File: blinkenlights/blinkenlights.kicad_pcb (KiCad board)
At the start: 4 copper layers, 160 x 100 mm, 158 parts, among them J201 Conn_03x32_Row_Letter_First, J301 Conn_01x01_Female, J302 Conn_01x01_Female, J303 Conn_01x01_Female, J304 Conn_01x01_Female, J501 Conn_ARM_SWD, J502 Conn_02x03_Odd_Even, SW101 Black, SW102 Orang, U104 74AUC2G07, U106 74HC2G14, U301 BD9C301FJ, U303 AMS1117-3.3, U401 74HC244, U402 74AUC2G34, U501 ATSAM4S8CB-AN, U502 PCA9306DP, U601 SN74LVCH16T245, U602 SN74LXC8T245, U603 SN74LVC2T45, U604 SN74LVC2T45, U605 SN74LVC2T45, U606 SN74LVCH16T245, U607 SN74LXC8T245, U608 74LVC2G06, U609 74LVC2G06, U610 74LVC2G06, U611 74LVC2G06

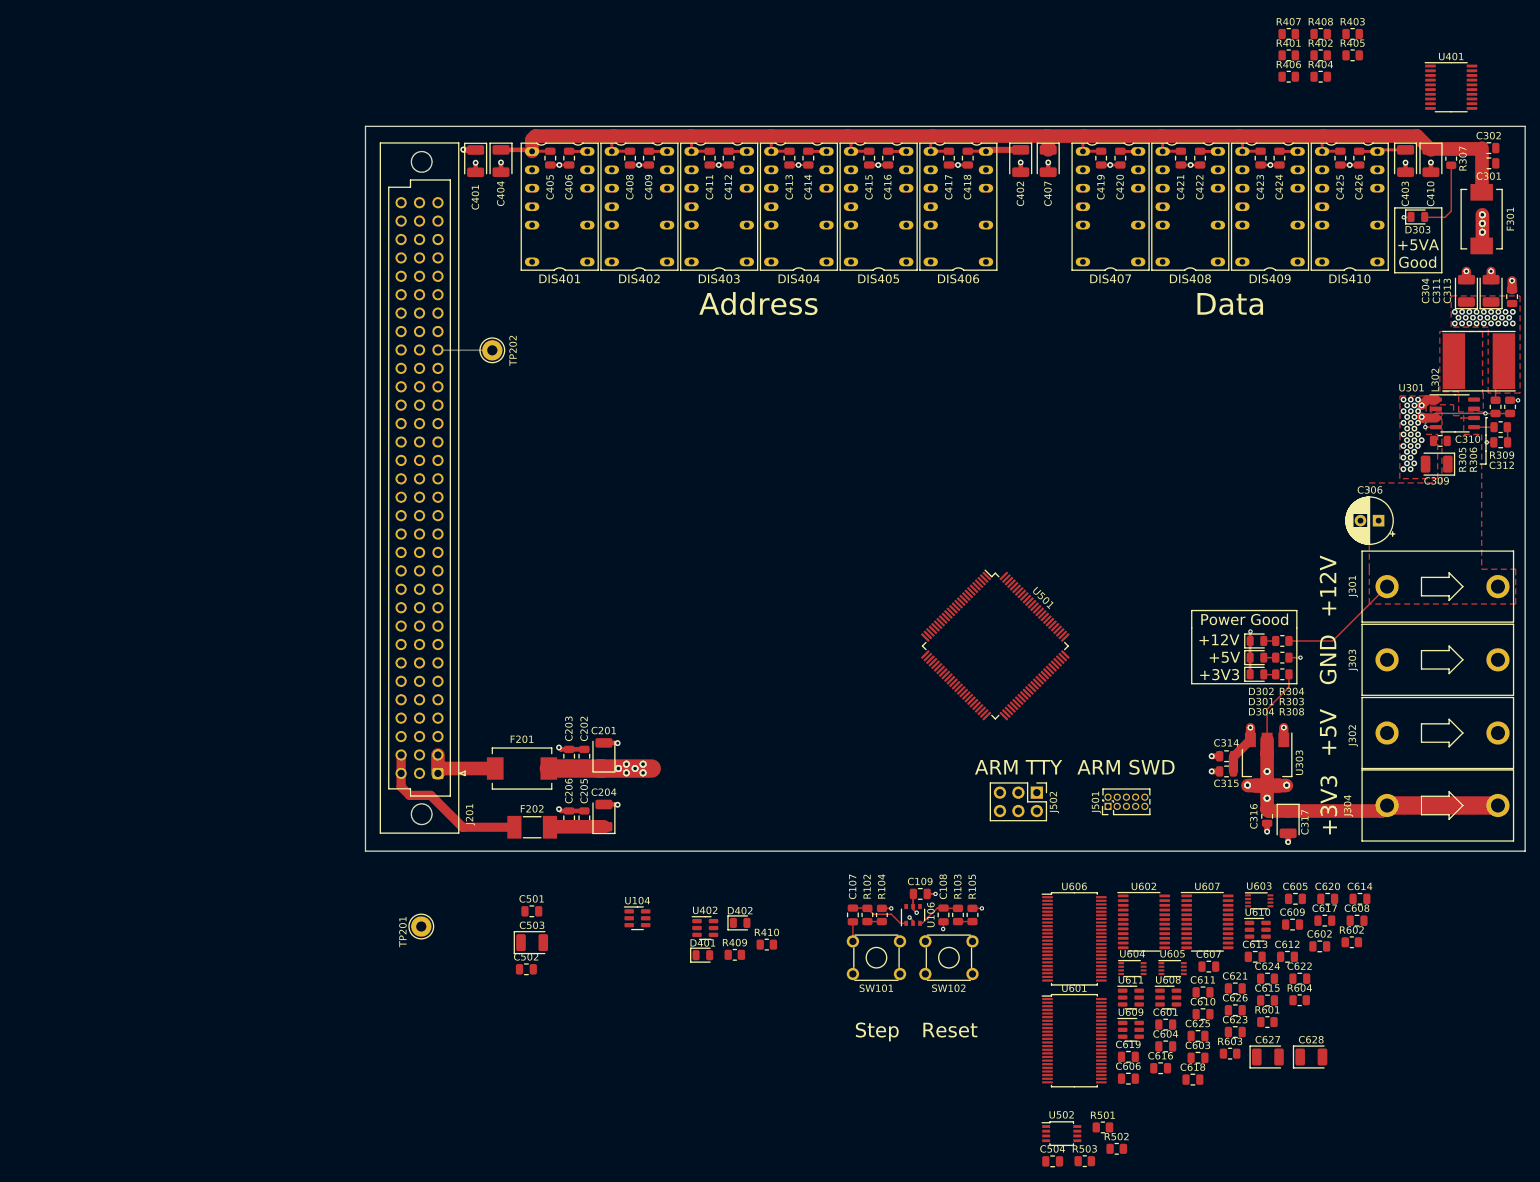
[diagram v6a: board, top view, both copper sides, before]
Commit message: Routed address/data bus on blinkenlights
- It goes to the funky hex display bois now and is routed so that it
  should be pretty ez to yeet on down into level shifters for the big
  ARM chip that runs the show
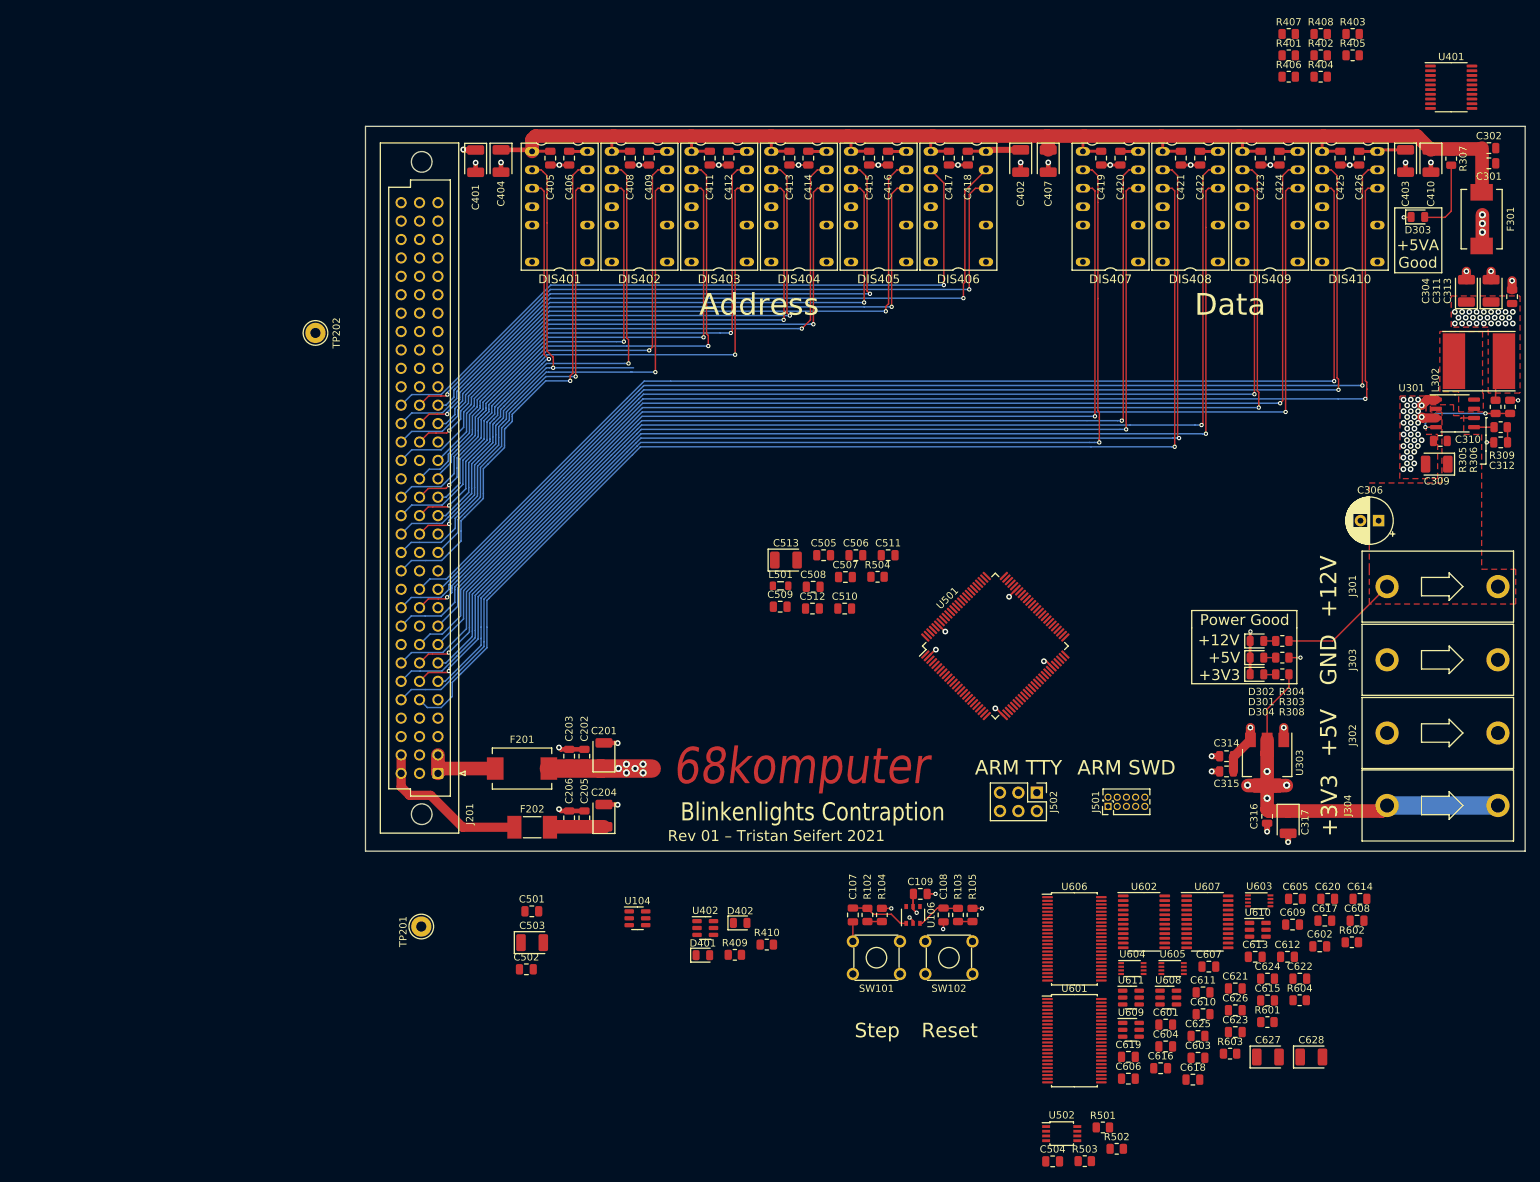
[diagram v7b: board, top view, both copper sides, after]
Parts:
- added C505: 100nF, Capacitor_SMD:C_0805_2012Metric, F.Cu at (83.2, 79.2)
- added C506: 100nF, Capacitor_SMD:C_0805_2012Metric, F.Cu at (87.7, 79.2)
- added C507: 100nF, Capacitor_SMD:C_0805_2012Metric, F.Cu at (86.2, 82.2)
- added C508: 4.7µF, Capacitor_SMD:C_0805_2012Metric, F.Cu at (81.8, 83.5)
- added C509: 4.7µF, Capacitor_SMD:C_0805_2012Metric, F.Cu at (77.2, 86.3)
- added C510: 100nF, Capacitor_SMD:C_0805_2012Metric, F.Cu at (86.1, 86.5)
- added C511: 100nF, Capacitor_SMD:C_0805_2012Metric, F.Cu at (92.1, 79.2)
- added C512: 4.7µF, Capacitor_SMD:C_0805_2012Metric, F.Cu at (81.7, 86.5)
- added C513: 10µF, Capacitor_Tantalum_SMD:CP_EIA-3528-21_Kemet-B, F.Cu at (78.0, 79.8)
- added L501: 10µH, Inductor_SMD:L_0805_2012Metric, F.Cu at (77.3, 83.4)
- added R504: 1R, Resistor_SMD:R_0805_2012Metric, F.Cu at (90.7, 82.2)
- moved TP202 24.5 mm to (13.1, 48.5)
- turned U501 to 45 degrees
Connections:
- DIS401 pad 12: /Displays and Indicators/A3 -> /A23
- DIS401 pad 13: /Displays and Indicators/A2 -> /A22
- DIS401 pad 2: /Displays and Indicators/A1 -> /A21
- DIS401 pad 3: GND -> /A20
- DIS402 pad 12: /Displays and Indicators/A7 -> /A19
- DIS402 pad 13: /Displays and Indicators/A6 -> /A18
- DIS402 pad 2: /Displays and Indicators/A5 -> /A17
- DIS402 pad 3: /Displays and Indicators/A4 -> /A16
- DIS403 pad 12: /Displays and Indicators/A11 -> /A15
- DIS403 pad 13: /Displays and Indicators/A10 -> /A14
- DIS403 pad 2: /Displays and Indicators/A9 -> /A13
- DIS403 pad 3: /Displays and Indicators/A8 -> /A12
- DIS404 pad 12: /Displays and Indicators/A15 -> /A11
- DIS404 pad 13: /Displays and Indicators/A14 -> /A10
- DIS404 pad 2: /Displays and Indicators/A13 -> /A9
- DIS404 pad 3: /Displays and Indicators/A12 -> /A8
- DIS405 pad 12: /Displays and Indicators/A19 -> /A7
- DIS405 pad 13: /Displays and Indicators/A18 -> /A6
- DIS405 pad 2: /Displays and Indicators/A17 -> /A5
- DIS405 pad 3: /Displays and Indicators/A16 -> /A4
- DIS406 pad 12: /Displays and Indicators/A23 -> /A3
- DIS406 pad 13: /Displays and Indicators/A22 -> /A2
- DIS406 pad 2: /Displays and Indicators/A21 -> /A1
- DIS406 pad 3: /Displays and Indicators/A20 -> GND
- DIS407 pad 12: /Displays and Indicators/D3 -> /D15
- DIS407 pad 13: /Displays and Indicators/D2 -> /D14
- DIS407 pad 2: /Displays and Indicators/D1 -> /D13
- DIS407 pad 3: /Displays and Indicators/D0 -> /D12
- DIS408 pad 10: Net-(DIS408-Pad10) -> Net-(R406-Pad1)
- DIS408 pad 12: /Displays and Indicators/D7 -> /D11
- DIS408 pad 13: /Displays and Indicators/D6 -> /D10
- DIS408 pad 2: /Displays and Indicators/D5 -> /D9
- DIS408 pad 3: /Displays and Indicators/D4 -> /D8
- DIS408 pad 4: Net-(DIS408-Pad4) -> Net-(R405-Pad1)
- DIS409 pad 12: /Displays and Indicators/D11 -> /D7
- DIS409 pad 13: /Displays and Indicators/D10 -> /D6
- DIS409 pad 2: /Displays and Indicators/D9 -> /D5
- DIS409 pad 3: /Displays and Indicators/D8 -> /D4
- DIS410 pad 10: Net-(DIS410-Pad10) -> Net-(R402-Pad1)
- DIS410 pad 12: /Displays and Indicators/D15 -> /D3
- DIS410 pad 13: /Displays and Indicators/D14 -> /D2
- DIS410 pad 2: /Displays and Indicators/D13 -> /D1
- DIS410 pad 3: /Displays and Indicators/D12 -> /D0
- DIS410 pad 4: Net-(DIS410-Pad4) -> Net-(R401-Pad1)
- J201 pad a11: /Backplane Connector/D2 -> /D2
- J201 pad a13: /Backplane Connector/A23 -> /A23
- J201 pad a15: /Backplane Connector/A20 -> /A20
- J201 pad a16: /Backplane Connector/A13 -> /A13
- J201 pad a17: /Backplane Connector/A14 -> /A14
- J201 pad a18: /Backplane Connector/A11 -> /A11
- J201 pad a20: /Backplane Connector/A7 -> /A7
- J201 pad a21: /Backplane Connector/A5 -> /A5
- J201 pad a6: /Backplane Connector/D9 -> /D9
- J201 pad a7: /Backplane Connector/D10 -> /D10
- J201 pad a8: /Backplane Connector/D7 -> /D7
- J201 pad a9: /Backplane Connector/D6 -> /D6
- J201 pad b10: /Backplane Connector/D4 -> /D4
- J201 pad b11: /Backplane Connector/D0 -> /D0
- J201 pad b14: /Backplane Connector/A21 -> /A21
- J201 pad b15: /Backplane Connector/A15 -> /A15
- J201 pad b16: /Backplane Connector/A16 -> /A16
- J201 pad b17: /Backplane Connector/A10 -> /A10
- J201 pad b19: /Backplane Connector/A9 -> /A9
- J201 pad b20: /Backplane Connector/A4 -> /A4
- J201 pad b21: /Backplane Connector/A3 -> /A3
- J201 pad b5: /Backplane Connector/D8 -> /D8
- J201 pad b6: /Backplane Connector/D11 -> /D11
- J201 pad b7: /Backplane Connector/D14 -> /D14
- J201 pad b8: /Backplane Connector/D5 -> /D5
- J201 pad c10: /Backplane Connector/D1 -> /D1
- J201 pad c12: /Backplane Connector/A22 -> /A22
- J201 pad c13: /Backplane Connector/A19 -> /A19
- J201 pad c14: /Backplane Connector/A17 -> /A17
- J201 pad c15: /Backplane Connector/A18 -> /A18
- J201 pad c16: /Backplane Connector/A12 -> /A12
- J201 pad c18: /Backplane Connector/A8 -> /A8
- J201 pad c19: /Backplane Connector/A6 -> /A6
- J201 pad c20: /Backplane Connector/A2 -> /A2
- J201 pad c21: /Backplane Connector/A1 -> /A1
- J201 pad c5: /Backplane Connector/D13 -> /D13
- J201 pad c6: /Backplane Connector/D15 -> /D15
- J201 pad c7: /Backplane Connector/D12 -> /D12
- J201 pad c9: /Backplane Connector/D3 -> /D3
- J501 pad 10: unconnected-(J501-Pad10) -> /Microcontroller/~{SWD_NRST}
- J501 pad 2: unconnected-(J501-Pad2) -> /Microcontroller/JTAG_TMS
- J501 pad 4: unconnected-(J501-Pad4) -> /Microcontroller/JTAG_TCK
- J501 pad 6: unconnected-(J501-Pad6) -> /Microcontroller/JTAG_TDO
- J501 pad 8: unconnected-(J501-Pad8) -> /Microcontroller/JTAG_TDI
- R401 pad 1: Net-(DIS407-Pad4) -> Net-(R401-Pad1)
- R402 pad 1: Net-(DIS407-Pad10) -> Net-(R402-Pad1)
- R403 pad 1: Net-(DIS408-Pad4) -> Net-(DIS409-Pad4)
- R404 pad 1: Net-(DIS408-Pad10) -> Net-(DIS409-Pad10)
- R405 pad 1: Net-(DIS409-Pad4) -> Net-(R405-Pad1)
- R406 pad 1: Net-(DIS409-Pad10) -> Net-(R406-Pad1)
- R407 pad 1: Net-(DIS410-Pad4) -> Net-(DIS407-Pad4)
- R408 pad 1: Net-(DIS410-Pad10) -> Net-(DIS407-Pad10)
- U501 pad 10: unconnected-(U501-Pad10) -> +3V3
- U501 pad 100: unconnected-(U501-Pad100) -> Net-(C506-Pad1)
- U501 pad 11: unconnected-(U501-Pad11) -> VDDCORE
- U501 pad 27: VDDIO -> +3V3
- U501 pad 50: VDDIO -> +3V3
- U501 pad 51: unconnected-(U501-Pad51) -> /Microcontroller/JTAG_TDI
- U501 pad 60: unconnected-(U501-Pad60) -> /Microcontroller/~{NRST}
- U501 pad 61: unconnected-(U501-Pad61) -> GND
- U501 pad 69: VDDIO -> +3V3
- U501 pad 76: unconnected-(U501-Pad76) -> /Microcontroller/JTAG_TDO
- U501 pad 79: unconnected-(U501-Pad79) -> /Microcontroller/JTAG_TMS
- U501 pad 83: unconnected-(U501-Pad83) -> /Microcontroller/JTAG_TCK
- U501 pad 91: VDDIO -> +3V3
- U501 pad 98: VDDIO -> +3V3
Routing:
- net /D3: track 0.00 -> 177.9 mm, vias 0 -> 1
- net /D1: track 0.00 -> 174.1 mm, vias 0 -> 1
- net /D2: track 0.00 -> 170.5 mm, vias 0 -> 1
- net /D0: track 0.00 -> 166.2 mm, vias 0 -> 1
- net /D5: track 0.00 -> 165.8 mm, vias 0 -> 1
- net /D7: track 0.00 -> 165.0 mm, vias 0 -> 1
- net /D6: track 0.00 -> 164.4 mm, vias 0 -> 1
- net /D8: track 0.00 -> 161.6 mm, vias 0 -> 1
- net /D11: track 0.00 -> 161.6 mm, vias 0 -> 2
- net /D10: track 0.00 -> 159.2 mm, vias 0 -> 1
- net /D9: track 0.00 -> 159.2 mm, vias 0 -> 1
- net /D4: track 0.00 -> 157.6 mm, vias 0 -> 2
- net /D13: track 0.00 -> 154.2 mm, vias 0 -> 1
- net /D15: track 0.00 -> 152.2 mm, vias 0 -> 1
- net /D14: track 0.00 -> 150.2 mm, vias 0 -> 2
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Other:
- board text added: "68komputer"
- board text added: "Blinkenlights Contraption"
- board text added: "Rev 01 – Tristan Seifert 2021"
